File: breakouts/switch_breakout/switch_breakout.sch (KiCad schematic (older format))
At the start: 10 parts

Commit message: work on breakouts
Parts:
- added U5: mounting_box, vna_footprints:POMONA_2400BOX, symbol mounting_box
- C1, C2, C3, C5: renamed from C?; footprint (none) -> Capacitors_SMD:C_0402
- C4: renamed from C?; footprint (none) -> Capacitors_SMD:C_0805
- P1: renamed from P?; footprint (none) -> Pin_Headers:Pin_Header_Straight_1x03
- U1, U2, U4: renamed from U?; footprint (none) -> vna_footprints:732512200_SMA
- U3: renamed from U?; footprint (none) -> Housings_DFN_QFN:QFN-16-1EP_3x3mm_Pitch0.5mm
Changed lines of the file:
@@
 LIBS:pe42521
 LIBS:conn_sma
+LIBS:mounting_box
+LIBS:switch_breakout-cache
 EELAYER 25 0
 EELAYER END
@@
 $EndDescr
 $Comp
-L PE42521 U?
+L PE42521 U3
 U 1 1 56AEE91C
 P 6350 4700
-F 0 "U?" H 5650 5250 60  0000 C CNN
+F 0 "U3" H 5650 5250 60  0000 C CNN
 F 1 "PE42521" H 5800 5350 60  0000 C CNN
-F 2 "" H 5650 5250 60  0000 C CNN
+F 2 "Housings_DFN_QFN:QFN-16-1EP_3x3mm_Pitch0.5mm" H 5650 5250 60  0001 C CNN
 F 3 "" H 5650 5250 60  0000 C CNN
 	1    6350 4700
@@
 $EndComp
 $Comp
-L C_Small C?
+L C_Small C5
 U 1 1 56AEE9AD
 P 8250 4650
-F 0 "C?" H 8260 4720 50  0000 L CNN
+F 0 "C5" H 8260 4720 50  0000 L CNN
 F 1 "C_Small" H 8260 4570 50  0000 L CNN
-F 2 "" H 8250 4650 50  0000 C CNN
+F 2 "Capacitors_SMD:C_0402" H 8250 4650 50  0001 C CNN
 F 3 "" H 8250 4650 50  0000 C CNN
 	1    8250 4650
@@
 $EndComp
 $Comp
-L CONN_SMA U?
+L CONN_SMA U4
 U 1 1 56AEE9D4
 P 9100 4650
-F 0 "U?" H 8750 4850 60  0000 C CNN
+F 0 "U4" H 8750 4850 60  0000 C CNN
 F 1 "CONN_SMA" H 8950 5000 60  0000 C CNN
-F 2 "" H 9100 4650 60  0000 C CNN
+F 2 "vna_footprints:732512200_SMA" H 9100 4650 60  0001 C CNN
 F 3 "" H 9100 4650 60  0000 C CNN
 	1    9100 4650
@@
 $EndComp
 $Comp
-L GND #PWR?
+L GND #PWR17
 U 1 1 56AEEAAA
 P 9100 5350
-F 0 "#PWR?" H 9100 5100 50  0001 C CNN
+F 0 "#PWR17" H 9100 5100 50  0001 C CNN
 F 1 "GND" H 9100 5200 50  0000 C CNN
 F 2 "" H 9100 5350 50  0000 C CNN
@@
 	3550 3350 6300 3350
 $Comp
-L C_Small C?
+L C_Small C2
 U 1 1 56AEF25D
 P 3450 5750
-F 0 "C?" H 3460 5820 50  0000 L CNN
+F 0 "C2" H 3460 5820 50  0000 L CNN
 F 1 "C_Small" H 3460 5670 50  0000 L CNN
-F 2 "" H 3450 5750 50  0000 C CNN
+F 2 "Capacitors_SMD:C_0402" H 3450 5750 50  0001 C CNN
 F 3 "" H 3450 5750 50  0000 C CNN
 	1    3450 5750
@@
 $EndComp
 $Comp
-L CONN_SMA U?
+L CONN_SMA U2
 U 1 1 56AEF263
 P 2600 5750
-F 0 "U?" H 2250 5950 60  0000 C CNN
+F 0 "U2" H 2250 5950 60  0000 C CNN
 F 1 "CONN_SMA" H 2450 6100 60  0000 C CNN
-F 2 "" H 2600 5750 60  0000 C CNN
+F 2 "vna_footprints:732512200_SMA" H 2600 5750 60  0001 C CNN
 F 3 "" H 2600 5750 60  0000 C CNN
 	1    2600 5750
@@
 $EndComp
 $Comp
-L GND #PWR?
+L GND #PWR2
 U 1 1 56AEF269
 P 2600 6450
-F 0 "#PWR?" H 2600 6200 50  0001 C CNN
+F 0 "#PWR2" H 2600 6200 50  0001 C CNN
 F 1 "GND" H 2600 6300 50  0000 C CNN
 F 2 "" H 2600 6450 50  0000 C CNN
@@
 	6300 5750 6300 5350
 $Comp
-L GND #PWR?
+L GND #PWR11
 U 1 1 56AEF357
 P 6400 5450
-F 0 "#PWR?" H 6400 5200 50  0001 C CNN
+F 0 "#PWR11" H 6400 5200 50  0001 C CNN
 F 1 "GND" H 6400 5300 50  0000 C CNN
 F 2 "" H 6400 5450 50  0000 C CNN
@@
 $EndComp
 $Comp
-L GND #PWR?
+L GND #PWR13
 U 1 1 56AEF39E
 P 6500 5450
-F 0 "#PWR?" H 6500 5200 50  0001 C CNN
+F 0 "#PWR13" H 6500 5200 50  0001 C CNN
 F 1 "GND" H 6500 5300 50  0000 C CNN
 F 2 "" H 6500 5450 50  0000 C CNN
@@
 $EndComp
 $Comp
-L GND #PWR?
+L GND #PWR9
 U 1 1 56AEF4BB
 P 6200 5450
-F 0 "#PWR?" H 6200 5200 50  0001 C CNN
+F 0 "#PWR9" H 6200 5200 50  0001 C CNN
 F 1 "GND" H 6200 5300 50  0000 C CNN
 F 2 "" H 6200 5450 50  0000 C CNN
@@
 	6500 5450 6500 5350
 $Comp
-L GND #PWR?
+L GND #PWR12
 U 1 1 56AEF535
 P 6500 3900
-F 0 "#PWR?" H 6500 3650 50  0001 C CNN
+F 0 "#PWR12" H 6500 3650 50  0001 C CNN
 F 1 "GND" H 6500 3750 50  0000 C CNN
 F 2 "" H 6500 3900 50  0000 C CNN
@@
 	6500 3900 6500 4050
 $Comp
-L GND #PWR?
+L GND #PWR10
 U 1 1 56AEF5AD
 P 6400 3900
-F 0 "#PWR?" H 6400 3650 50  0001 C CNN
+F 0 "#PWR10" H 6400 3650 50  0001 C CNN
 F 1 "GND" H 6400 3750 50  0000 C CNN
 F 2 "" H 6400 3900 50  0000 C CNN
@@
 	6400 3900 6400 4050
 $Comp
-L GND #PWR?
+L GND #PWR8
 U 1 1 56AEF5EA
 P 6200 3900
-F 0 "#PWR?" H 6200 3650 50  0001 C CNN
+F 0 "#PWR8" H 6200 3650 50  0001 C CNN
 F 1 "GND" H 6200 3750 50  0000 C CNN
 F 2 "" H 6200 3900 50  0000 C CNN
@@
 	6200 3900 6200 4050
 $Comp
-L GND #PWR?
+L GND #PWR14
 U 1 1 56AEF628
 P 7100 4550
-F 0 "#PWR?" H 7100 4300 50  0001 C CNN
+F 0 "#PWR14" H 7100 4300 50  0001 C CNN
 F 1 "GND" H 7100 4400 50  0000 C CNN
 F 2 "" H 7100 4550 50  0000 C CNN
@@
 	7000 4550 7100 4550
 $Comp
-L GND #PWR?
+L GND #PWR15
 U 1 1 56AEF667
 P 7100 4750
-F 0 "#PWR?" H 7100 4500 50  0001 C CNN
+F 0 "#PWR15" H 7100 4500 50  0001 C CNN
 F 1 "GND" H 7100 4600 50  0000 C CNN
 F 2 "" H 7100 4750 50  0000 C CNN
@@
 	7100 4750 7000 4750
 $Comp
-L GND #PWR?
+L GND #PWR16
 U 1 1 56AEF6A7
 P 7100 4850
-F 0 "#PWR?" H 7100 4600 50  0001 C CNN
+F 0 "#PWR16" H 7100 4600 50  0001 C CNN
 F 1 "GND" H 7100 4700 50  0000 C CNN
 F 2 "" H 7100 4850 50  0000 C CNN
@@
 	7100 4850 7000 4850
 $Comp
-L GND #PWR?
+L GND #PWR6
 U 1 1 56AEF70C
 P 5600 4550
-F 0 "#PWR?" H 5600 4300 50  0001 C CNN
+F 0 "#PWR6" H 5600 4300 50  0001 C CNN
 F 1 "GND" H 5600 4400 50  0000 C CNN
 F 2 "" H 5600 4550 50  0000 C CNN
@@
 	5600 4550 5700 4550
 $Comp
-L GND #PWR?
+L GND #PWR7
 U 1 1 56AEF771
 P 5600 4750
-F 0 "#PWR?" H 5600 4500 50  0001 C CNN
+F 0 "#PWR7" H 5600 4500 50  0001 C CNN
 F 1 "GND" H 5600 4600 50  0000 C CNN
 F 2 "" H 5600 4750 50  0000 C CNN
@@
 	7000 4650 8150 4650
 $Comp
-L C_Small C?
+L C_Small C1
 U 1 1 56AF189D
 P 3450 3350
-F 0 "C?" H 3460 3420 50  0000 L CNN
+F 0 "C1" H 3460 3420 50  0000 L CNN
 F 1 "C_Small" H 3460 3270 50  0000 L CNN
-F 2 "" H 3450 3350 50  0000 C CNN
+F 2 "Capacitors_SMD:C_0402" H 3450 3350 50  0001 C CNN
 F 3 "" H 3450 3350 50  0000 C CNN
 	1    3450 3350
@@
 $EndComp
 $Comp
-L CONN_SMA U?
+L CONN_SMA U1
 U 1 1 56AF18A3
 P 2600 3350
-F 0 "U?" H 2250 3550 60  0000 C CNN
+F 0 "U1" H 2250 3550 60  0000 C CNN
 F 1 "CONN_SMA" H 2450 3700 60  0000 C CNN
-F 2 "" H 2600 3350 60  0000 C CNN
+F 2 "vna_footprints:732512200_SMA" H 2600 3350 60  0001 C CNN
 F 3 "" H 2600 3350 60  0000 C CNN
 	1    2600 3350
@@
 $EndComp
 $Comp
-L GND #PWR?
+L GND #PWR1
 U 1 1 56AF18A9
 P 2600 4050
-F 0 "#PWR?" H 2600 3800 50  0001 C CNN
+F 0 "#PWR1" H 2600 3800 50  0001 C CNN
 F 1 "GND" H 2600 3900 50  0000 C CNN
 F 2 "" H 2600 4050 50  0000 C CNN
@@
 	3350 3350 3150 3350
 $Comp
-L CONN_01X03 P?
+L CONN_01X03 P1
 U 1 1 56AF18F1
 P 4200 4750
-F 0 "P?" H 4200 4950 50  0000 C CNN
+F 0 "P1" H 4200 4950 50  0000 C CNN
 F 1 "CONN_01X03" V 4300 4750 50  0000 C CNN
-F 2 "" H 4200 4750 50  0000 C CNN
+F 2 "Pin_Headers:Pin_Header_Straight_1x03" H 4200 4750 50  0001 C CNN
 F 3 "" H 4200 4750 50  0000 C CNN
 	1    4200 4750
@@
 	5700 4850 4400 4850
 $Comp
-L GND #PWR?
+L GND #PWR3
 U 1 1 56AF1A38
 P 4550 4750
-F 0 "#PWR?" H 4550 4500 50  0001 C CNN
+F 0 "#PWR3" H 4550 4500 50  0001 C CNN
 F 1 "GND" H 4550 4600 50  0000 C CNN
 F 2 "" H 4550 4750 50  0000 C CNN
@@
 	4550 4750 4400 4750
 $Comp
-L C_Small C?
+L C_Small C3
 U 1 1 56AF1ADD
 P 4650 5100
-F 0 "C?" H 4660 5170 50  0000 L CNN
+F 0 "C3" H 4660 5170 50  0000 L CNN
 F 1 "C_Small" H 4660 5020 50  0000 L CNN
-F 2 "" H 4650 5100 50  0000 C CNN
+F 2 "Capacitors_SMD:C_0402" H 4650 5100 50  0001 C CNN
 F 3 "" H 4650 5100 50  0000 C CNN
 	1    4650 5100
@@
 $EndComp
 $Comp
-L C_Small C?
+L C_Small C4
 U 1 1 56AF1B50
 P 5000 5100
-F 0 "C?" H 5010 5170 50  0000 L CNN
+F 0 "C4" H 5010 5170 50  0000 L CNN
 F 1 "C_Small" H 5010 5020 50  0000 L CNN
-F 2 "" H 5000 5100 50  0000 C CNN
+F 2 "Capacitors_SMD:C_0805" H 5000 5100 50  0001 C CNN
 F 3 "" H 5000 5100 50  0000 C CNN
 	1    5000 5100
@@
 $EndComp
 $Comp
-L GND #PWR?
+L GND #PWR4
 U 1 1 56AF1B84
 P 4650 5300
-F 0 "#PWR?" H 4650 5050 50  0001 C CNN
+F 0 "#PWR4" H 4650 5050 50  0001 C CNN
 F 1 "GND" H 4650 5150 50  0000 C CNN
 F 2 "" H 4650 5300 50  0000 C CNN
@@
 Connection ~ 4650 4850
 $Comp
-L GND #PWR?
+L GND #PWR5
 U 1 1 56AF1C5F
 P 5000 5300
-F 0 "#PWR?" H 5000 5050 50  0001 C CNN
+F 0 "#PWR5" H 5000 5050 50  0001 C CNN
 F 1 "GND" H 5000 5150 50  0000 C CNN
 F 2 "" H 5000 5300 50  0000 C CNN
@@
 	5000 4850 5000 5000
 Connection ~ 5000 4850
+$Comp
+L mounting_box U5
+U 1 1 56B63F52
+P 6250 2550
+F 0 "U5" H 6250 2550 60  0000 C CNN
+F 1 "mounting_box" H 6200 2700 60  0000 C CNN
+F 2 "vna_footprints:POMONA_2400BOX" H 6250 2550 60  0001 C CNN
+F 3 "" H 6250 2550 60  0000 C CNN
+	1    6250 2550
+	1    0    0    -1
+$EndComp
 $EndSCHEMATC

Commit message: layout of splitter, switch, and filter
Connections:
- net GND: now also U3.17 (GND)
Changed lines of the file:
@@
 $EndComp
 $Comp
-L GND #PWR17
+L GND #PWR01
 U 1 1 56AEEAAA
 P 9100 5350
-F 0 "#PWR17" H 9100 5100 50  0001 C CNN
+F 0 "#PWR01" H 9100 5100 50  0001 C CNN
 F 1 "GND" H 9100 5200 50  0000 C CNN
 F 2 "" H 9100 5350 50  0000 C CNN
@@
 $EndComp
 $Comp
-L GND #PWR2
+L GND #PWR02
 U 1 1 56AEF269
 P 2600 6450
-F 0 "#PWR2" H 2600 6200 50  0001 C CNN
+F 0 "#PWR02" H 2600 6200 50  0001 C CNN
 F 1 "GND" H 2600 6300 50  0000 C CNN
 F 2 "" H 2600 6450 50  0000 C CNN
@@
 	6300 5750 6300 5350
 $Comp
-L GND #PWR11
+L GND #PWR03
 U 1 1 56AEF357
 P 6400 5450
-F 0 "#PWR11" H 6400 5200 50  0001 C CNN
+F 0 "#PWR03" H 6400 5200 50  0001 C CNN
 F 1 "GND" H 6400 5300 50  0000 C CNN
 F 2 "" H 6400 5450 50  0000 C CNN
@@
 $EndComp
 $Comp
-L GND #PWR13
+L GND #PWR04
 U 1 1 56AEF39E
 P 6500 5450
-F 0 "#PWR13" H 6500 5200 50  0001 C CNN
+F 0 "#PWR04" H 6500 5200 50  0001 C CNN
 F 1 "GND" H 6500 5300 50  0000 C CNN
 F 2 "" H 6500 5450 50  0000 C CNN
@@
 $EndComp
 $Comp
-L GND #PWR9
+L GND #PWR05
 U 1 1 56AEF4BB
 P 6200 5450
-F 0 "#PWR9" H 6200 5200 50  0001 C CNN
+F 0 "#PWR05" H 6200 5200 50  0001 C CNN
 F 1 "GND" H 6200 5300 50  0000 C CNN
 F 2 "" H 6200 5450 50  0000 C CNN
@@
 	6500 5450 6500 5350
 $Comp
-L GND #PWR12
+L GND #PWR06
 U 1 1 56AEF535
 P 6500 3900
-F 0 "#PWR12" H 6500 3650 50  0001 C CNN
+F 0 "#PWR06" H 6500 3650 50  0001 C CNN
 F 1 "GND" H 6500 3750 50  0000 C CNN
 F 2 "" H 6500 3900 50  0000 C CNN
@@
 	6500 3900 6500 4050
 $Comp
-L GND #PWR10
+L GND #PWR07
 U 1 1 56AEF5AD
 P 6400 3900
-F 0 "#PWR10" H 6400 3650 50  0001 C CNN
+F 0 "#PWR07" H 6400 3650 50  0001 C CNN
 F 1 "GND" H 6400 3750 50  0000 C CNN
 F 2 "" H 6400 3900 50  0000 C CNN
@@
 	6400 3900 6400 4050
 $Comp
-L GND #PWR8
+L GND #PWR08
 U 1 1 56AEF5EA
 P 6200 3900
-F 0 "#PWR8" H 6200 3650 50  0001 C CNN
+F 0 "#PWR08" H 6200 3650 50  0001 C CNN
 F 1 "GND" H 6200 3750 50  0000 C CNN
 F 2 "" H 6200 3900 50  0000 C CNN
@@
 	6200 3900 6200 4050
 $Comp
-L GND #PWR14
+L GND #PWR09
 U 1 1 56AEF628
 P 7100 4550
-F 0 "#PWR14" H 7100 4300 50  0001 C CNN
+F 0 "#PWR09" H 7100 4300 50  0001 C CNN
 F 1 "GND" H 7100 4400 50  0000 C CNN
 F 2 "" H 7100 4550 50  0000 C CNN
@@
 	7000 4550 7100 4550
 $Comp
-L GND #PWR15
+L GND #PWR010
 U 1 1 56AEF667
 P 7100 4750
-F 0 "#PWR15" H 7100 4500 50  0001 C CNN
+F 0 "#PWR010" H 7100 4500 50  0001 C CNN
 F 1 "GND" H 7100 4600 50  0000 C CNN
 F 2 "" H 7100 4750 50  0000 C CNN
@@
 	7100 4750 7000 4750
 $Comp
-L GND #PWR16
+L GND #PWR011
 U 1 1 56AEF6A7
 P 7100 4850
-F 0 "#PWR16" H 7100 4600 50  0001 C CNN
+F 0 "#PWR011" H 7100 4600 50  0001 C CNN
 F 1 "GND" H 7100 4700 50  0000 C CNN
 F 2 "" H 7100 4850 50  0000 C CNN
@@
 	7100 4850 7000 4850
 $Comp
-L GND #PWR6
+L GND #PWR012
 U 1 1 56AEF70C
 P 5600 4550
-F 0 "#PWR6" H 5600 4300 50  0001 C CNN
+F 0 "#PWR012" H 5600 4300 50  0001 C CNN
 F 1 "GND" H 5600 4400 50  0000 C CNN
 F 2 "" H 5600 4550 50  0000 C CNN
@@
 	5600 4550 5700 4550
 $Comp
-L GND #PWR7
+L GND #PWR013
 U 1 1 56AEF771
 P 5600 4750
-F 0 "#PWR7" H 5600 4500 50  0001 C CNN
+F 0 "#PWR013" H 5600 4500 50  0001 C CNN
 F 1 "GND" H 5600 4600 50  0000 C CNN
 F 2 "" H 5600 4750 50  0000 C CNN
@@
 $EndComp
 $Comp
-L GND #PWR1
+L GND #PWR014
 U 1 1 56AF18A9
 P 2600 4050
-F 0 "#PWR1" H 2600 3800 50  0001 C CNN
+F 0 "#PWR014" H 2600 3800 50  0001 C CNN
 F 1 "GND" H 2600 3900 50  0000 C CNN
 F 2 "" H 2600 4050 50  0000 C CNN
@@
 	5700 4850 4400 4850
 $Comp
-L GND #PWR3
+L GND #PWR015
 U 1 1 56AF1A38
 P 4550 4750
-F 0 "#PWR3" H 4550 4500 50  0001 C CNN
+F 0 "#PWR015" H 4550 4500 50  0001 C CNN
 F 1 "GND" H 4550 4600 50  0000 C CNN
 F 2 "" H 4550 4750 50  0000 C CNN
@@
 $EndComp
 $Comp
-L GND #PWR4
+L GND #PWR016
 U 1 1 56AF1B84
 P 4650 5300
-F 0 "#PWR4" H 4650 5050 50  0001 C CNN
+F 0 "#PWR016" H 4650 5050 50  0001 C CNN
 F 1 "GND" H 4650 5150 50  0000 C CNN
 F 2 "" H 4650 5300 50  0000 C CNN
@@
 Connection ~ 4650 4850
 $Comp
-L GND #PWR5
+L GND #PWR017
 U 1 1 56AF1C5F
 P 5000 5300
-F 0 "#PWR5" H 5000 5050 50  0001 C CNN
+F 0 "#PWR017" H 5000 5050 50  0001 C CNN
 F 1 "GND" H 5000 5150 50  0000 C CNN
 F 2 "" H 5000 5300 50  0000 C CNN
@@
 	1    0    0    -1
 $EndComp
+$Comp
+L GND #PWR018
+U 1 1 56CE6531
+P 7100 4450
+F 0 "#PWR018" H 7100 4200 50  0001 C CNN
+F 1 "GND" H 7100 4300 50  0000 C CNN
+F 2 "" H 7100 4450 50  0000 C CNN
+F 3 "" H 7100 4450 50  0000 C CNN
+	1    7100 4450
+	0    -1   1    0
+$EndComp
+Wire Wire Line
+	7100 4450 7000 4450
 $EndSCHEMATC

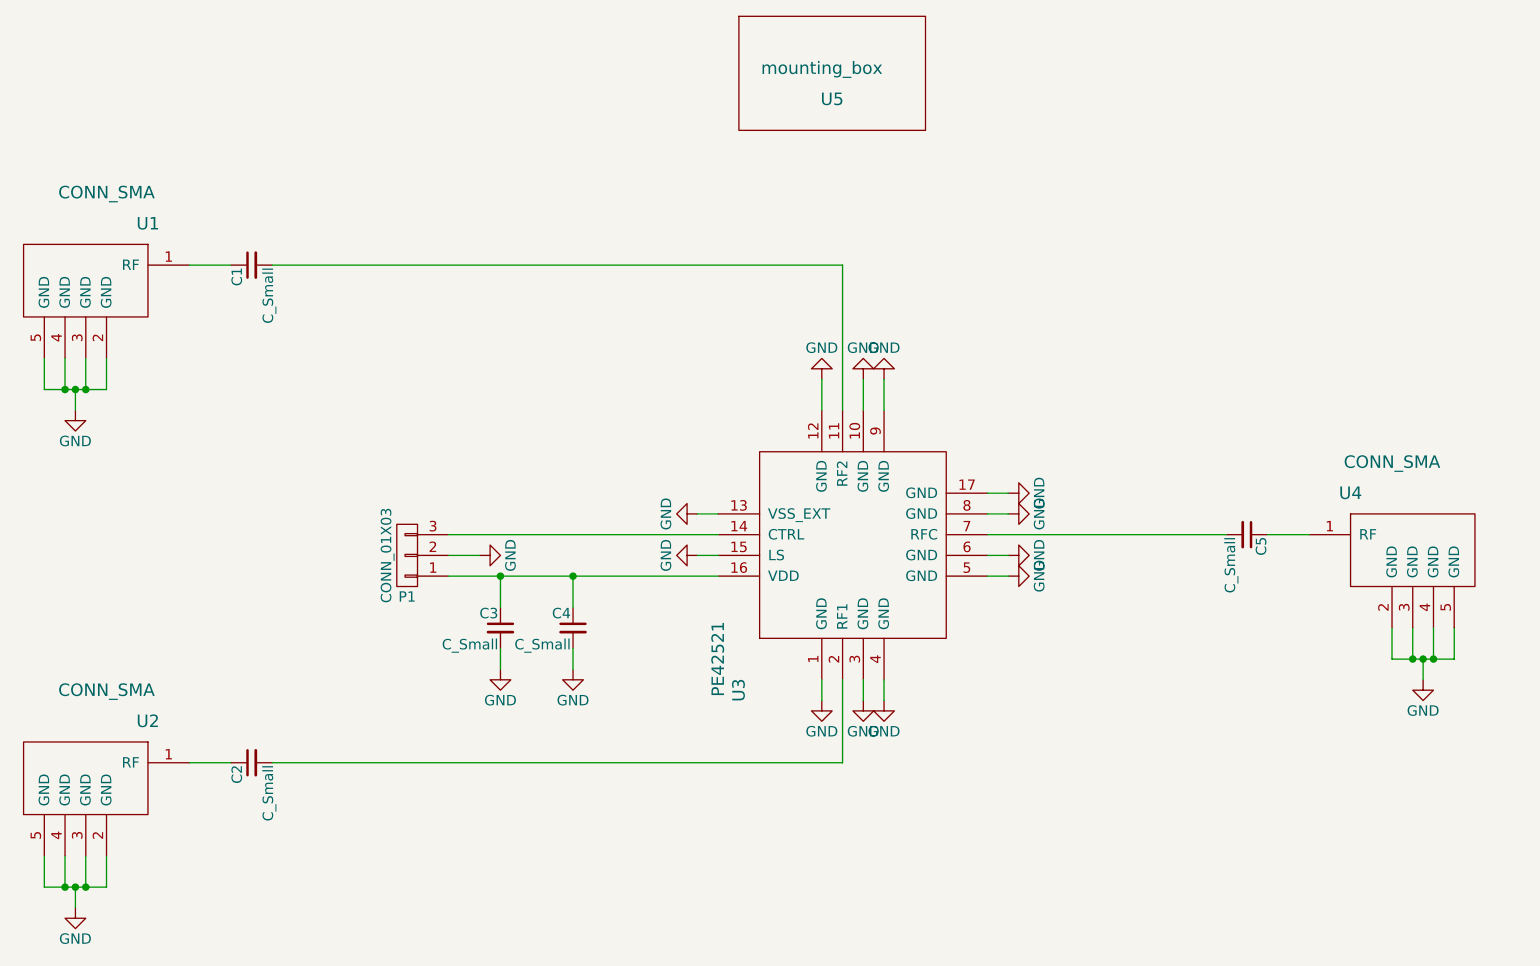
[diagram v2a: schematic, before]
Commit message: started variable attenuator, revised synth, and added power splittert to detect board
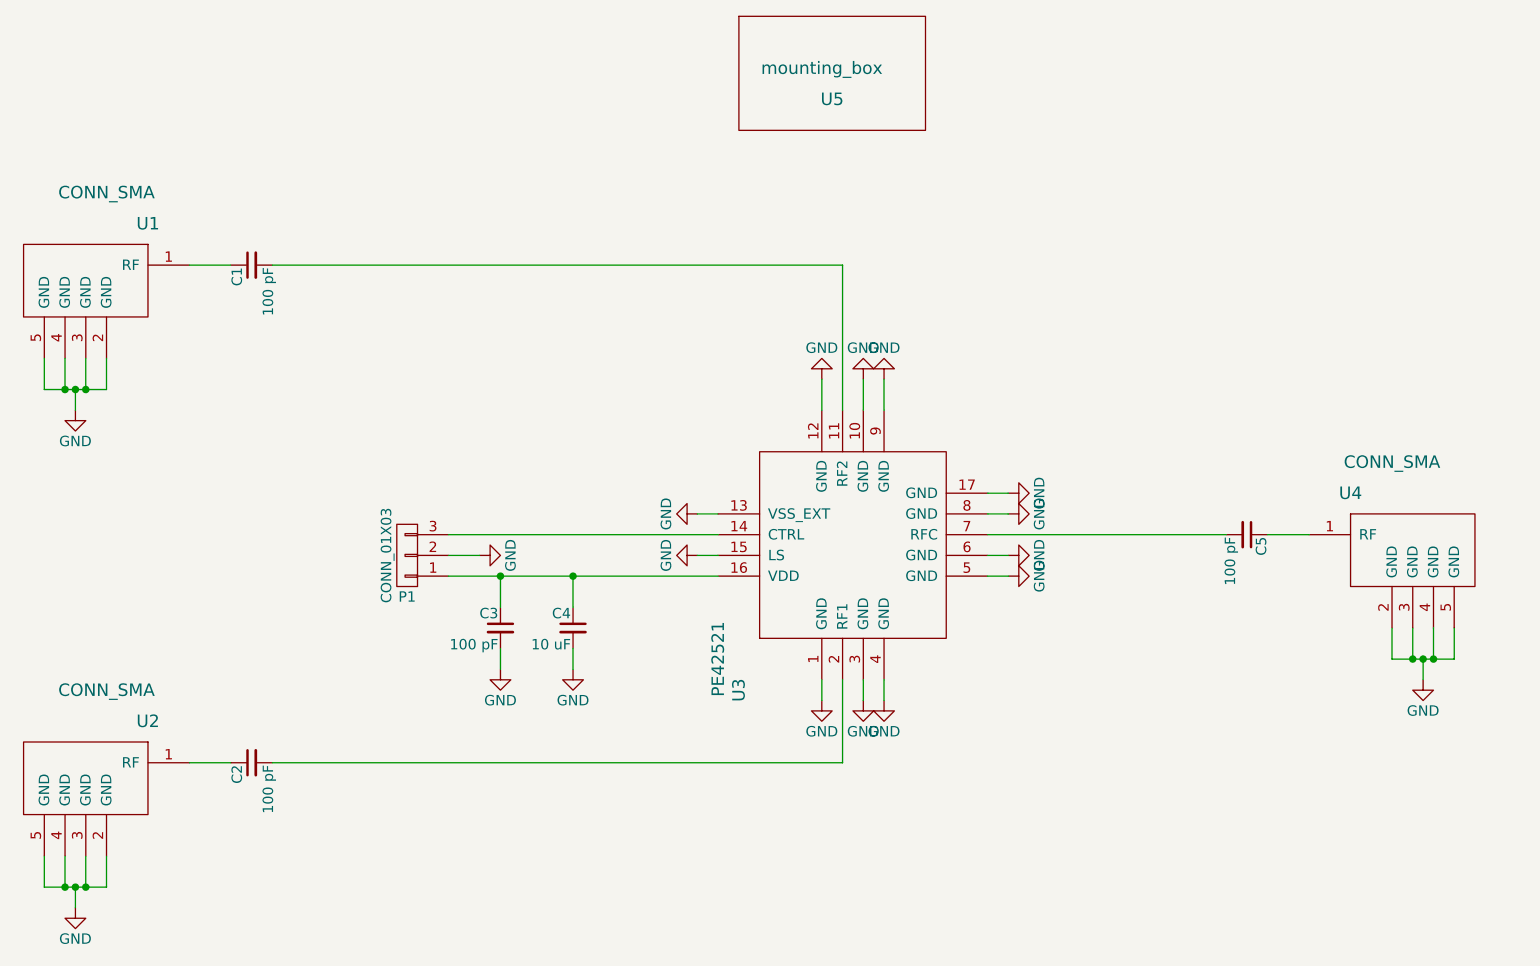
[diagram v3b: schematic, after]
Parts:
- C1, C2, C3, C5: value C_Small -> 100 pF
- C4: value C_Small -> 10 uF
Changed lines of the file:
@@
 P 8250 4650
 F 0 "C5" H 8260 4720 50  0000 L CNN
-F 1 "C_Small" H 8260 4570 50  0000 L CNN
+F 1 "100 pF" H 8260 4570 50  0000 L CNN
 F 2 "Capacitors_SMD:C_0402" H 8250 4650 50  0001 C CNN
 F 3 "" H 8250 4650 50  0000 C CNN
@@
 P 3450 5750
 F 0 "C2" H 3460 5820 50  0000 L CNN
-F 1 "C_Small" H 3460 5670 50  0000 L CNN
+F 1 "100 pF" H 3460 5670 50  0000 L CNN
 F 2 "Capacitors_SMD:C_0402" H 3450 5750 50  0001 C CNN
 F 3 "" H 3450 5750 50  0000 C CNN
@@
 P 3450 3350
 F 0 "C1" H 3460 3420 50  0000 L CNN
-F 1 "C_Small" H 3460 3270 50  0000 L CNN
+F 1 "100 pF" H 3460 3270 50  0000 L CNN
 F 2 "Capacitors_SMD:C_0402" H 3450 3350 50  0001 C CNN
 F 3 "" H 3450 3350 50  0000 C CNN
@@
 P 4650 5100
 F 0 "C3" H 4660 5170 50  0000 L CNN
-F 1 "C_Small" H 4660 5020 50  0000 L CNN
+F 1 "100 pF" H 4660 5020 50  0000 L CNN
 F 2 "Capacitors_SMD:C_0402" H 4650 5100 50  0001 C CNN
 F 3 "" H 4650 5100 50  0000 C CNN
@@
 P 5000 5100
 F 0 "C4" H 5010 5170 50  0000 L CNN
-F 1 "C_Small" H 5010 5020 50  0000 L CNN
+F 1 "10 uF" H 5010 5020 50  0000 L CNN
 F 2 "Capacitors_SMD:C_0805" H 5000 5100 50  0001 C CNN
 F 3 "" H 5000 5100 50  0000 C CNN

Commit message: trimmed ground plane on some breakouts so it doesn't disappear during panelization..
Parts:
- U1, U2, U4: footprint vna_footprints:732512200_SMA -> vna_footprints:732511150_sma
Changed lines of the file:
@@
 F 0 "U4" H 8750 4850 60  0000 C CNN
 F 1 "CONN_SMA" H 8950 5000 60  0000 C CNN
-F 2 "vna_footprints:732512200_SMA" H 9100 4650 60  0001 C CNN
+F 2 "vna_footprints:732511150_sma" H 9100 4650 60  0001 C CNN
 F 3 "" H 9100 4650 60  0000 C CNN
 	1    9100 4650
@@
 F 0 "U2" H 2250 5950 60  0000 C CNN
 F 1 "CONN_SMA" H 2450 6100 60  0000 C CNN
-F 2 "vna_footprints:732512200_SMA" H 2600 5750 60  0001 C CNN
+F 2 "vna_footprints:732511150_sma" H 2600 5750 60  0001 C CNN
 F 3 "" H 2600 5750 60  0000 C CNN
 	1    2600 5750
@@
 F 0 "U1" H 2250 3550 60  0000 C CNN
 F 1 "CONN_SMA" H 2450 3700 60  0000 C CNN
-F 2 "vna_footprints:732512200_SMA" H 2600 3350 60  0001 C CNN
+F 2 "vna_footprints:732511150_sma" H 2600 3350 60  0001 C CNN
 F 3 "" H 2600 3350 60  0000 C CNN
 	1    2600 3350
